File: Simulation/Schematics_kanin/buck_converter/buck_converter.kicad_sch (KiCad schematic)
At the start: 9 parts

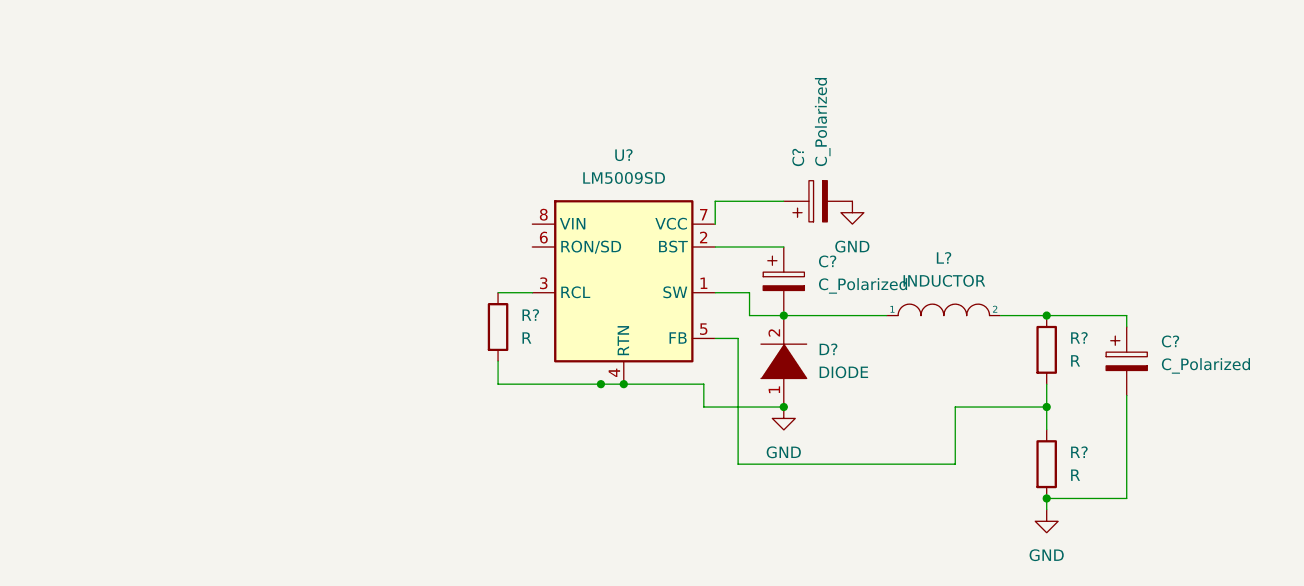
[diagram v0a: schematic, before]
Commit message: Nearly done with 7V MCU ckt, need to size output cap
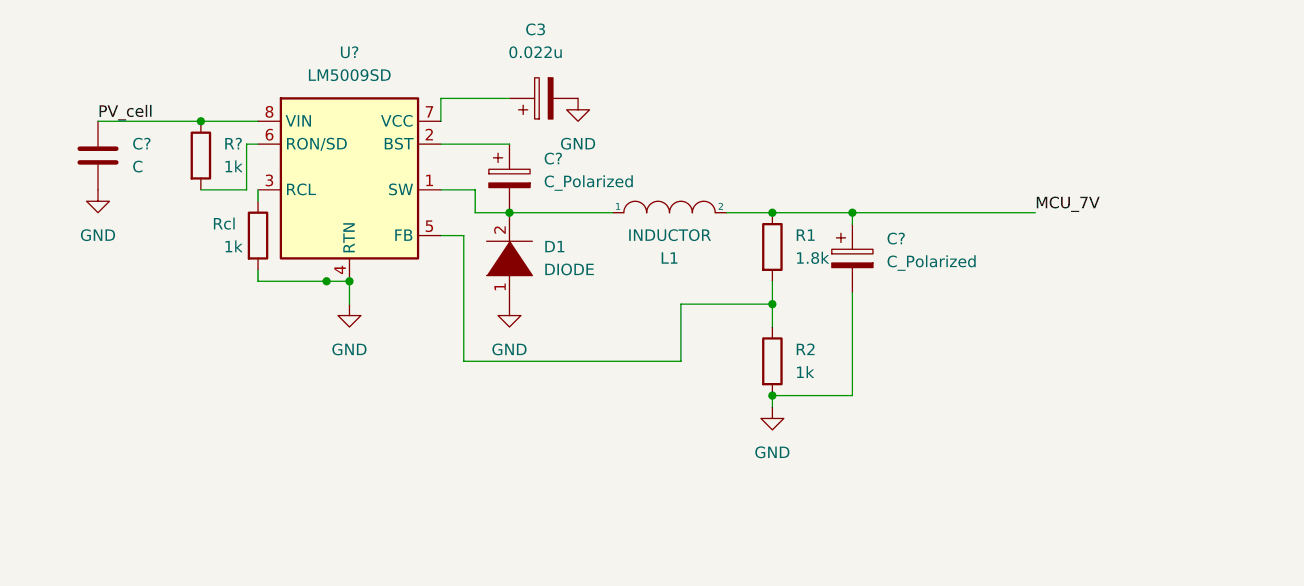
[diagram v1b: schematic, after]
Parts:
- added C?: C, symbol Device:C
- added R?: 1k, symbol Device:R
- C3: renamed from C?; value C_Polarized -> 0.022u
- R1: renamed from R?; value R -> 1.8k
- R2, Rcl: renamed from R?; value R -> 1k
- gave numbers to parts that had none: 2
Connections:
- net GND: now also C?.2
- net at U?.6 (RON/SD): now also R?.2
- net PV_cell: now reaches U?.8 (VIN)
- net PV_cell: now also C?.1, R?.1
- net MCU_7V: now reaches C?.1, L1.2, R1.1
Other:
- moved on the sheet: C3, C?, D1, L1, R1, R2, Rcl, U?

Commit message: Added a few values to schematic
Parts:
- removed C3: 0.022u, symbol Device:C_Polarized
- removed C? (x2): C_Polarized, symbol Device:C_Polarized
- added C2: C, symbol Device:C
- added C3: 0.1u, symbol Device:C
- added C4: 0.022u, symbol Device:C
- C1: renamed from C?; value C -> 0.022u
- gave numbers to parts that had none: 2
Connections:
- net GND: now also C2.2, C3.2
- net MCU_7V: now also C2.1
- net at D1.2 (A), L1.1, U1.1 (SW): now also C4.2
- net at U1.2 (BST): now also C4.1
- net at U1.7 (VCC): now also C3.1
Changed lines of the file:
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@@
     (stroke (width 0) (type default) (color 0 0 0 0))
   )
-  (wire (pts (xy 95.25 128.27) (xy 102.87 128.27))
+  (wire (pts (xy 95.25 128.27) (xy 99.06 128.27))
     (stroke (width 0) (type default) (color 0 0 0 0))
   )
@@
   )
   (wire (pts (xy 102.87 140.97) (xy 114.3 140.97))
+    (stroke (width 0) (type default) (color 0 0 0 0))
+  )
+  (wire (pts (xy 106.68 128.27) (xy 110.49 128.27))
     (stroke (width 0) (type default) (color 0 0 0 0))
   )
@@
   (symbol (lib_id "Regulator_Switching:LM5009SD") (at 85.09 135.89 0) (unit 1)
     (in_bom yes) (on_board yes) (fields_autoplaced)
-    (property "Reference" "U?" (id 0) (at 85.09 123.19 0))
+    (property "Reference" "U1" (id 0) (at 85.09 123.19 0))
     (property "Value" "LM5009SD" (id 1) (at 85.09 125.73 0))
     (property "Footprint" "Package_SON:WSON-8-1EP_4x4mm_P0.8mm_EP2.6x3mm" (id 2) (at 86.36 147.32 0)
@@
   )
   (symbol (lib_id "Device:R") (at 68.58 134.62 0) (unit 1)
-    (in_bom yes) (on_board yes) (fields_autoplaced)
-    (property "Reference" "R?" (id 0) (at 71.12 133.3499 0)
-      (effects (font (size 1.27 1.27)) (justify left))
-    )
-    (property "Value" "1k" (id 1) (at 71.12 135.8899 0)
+    (in_bom yes) (on_board yes)
+    (property "Reference" "Ron" (id 0) (at 63.5 133.3501 0)
+      (effects (font (size 1.27 1.27)) (justify left))
+    )
+    (property "Value" "1k" (id 1) (at 64.77 135.89 0)
       (effects (font (size 1.27 1.27)) (justify left))
     )
@@
     (pin "2")
   )
+  (symbol (lib_id "Device:C") (at 102.87 137.16 0) (unit 1)
+    (in_bom yes) (on_board yes) (fields_autoplaced)
+    (property "Reference" "C4" (id 0) (at 106.68 135.8899 0)
+      (effects (font (size 1.27 1.27)) (justify left))
+    )
+    (property "Value" "0.022u" (id 1) (at 106.68 138.4299 0)
+      (effects (font (size 1.27 1.27)) (justify left))
+    )
+    (property "Footprint" "" (id 2) (at 103.8352 140.97 0)
+      (effects (font (size 1.27 1.27)) hide)
+    )
+    (property "Datasheet" "~" (id 3) (at 102.87 137.16 0)
+      (effects (font (size 1.27 1.27)) hide)
+    )
+    (pin "1")
+    (pin "2")
+  )
   (symbol (lib_id "Device:R") (at 132.08 157.48 0) (unit 1)
     (in_bom yes) (on_board yes) (fields_autoplaced)
@@
     )
     (property "Datasheet" "~" (id 3) (at 132.08 157.48 0)
-      (effects (font (size 1.27 1.27)) hide)
-    )
-    (pin "1")
-    (pin "2")
-  )
-  (symbol (lib_id "Device:C_Polarized") (at 106.68 128.27 90) (unit 1)
-    (in_bom yes) (on_board yes) (fields_autoplaced)
-    (property "Reference" "C3" (id 0) (at 105.791 120.65 90))
-    (property "Value" "0.022u" (id 1) (at 105.791 123.19 90))
-    (property "Footprint" "" (id 2) (at 110.49 127.3048 0)
-      (effects (font (size 1.27 1.27)) hide)
-    )
-    (property "Datasheet" "~" (id 3) (at 106.68 128.27 0)
       (effects (font (size 1.27 1.27)) hide)
     )
@@
   )
   (symbol (lib_id "power:GND") (at 110.49 128.27 0) (unit 1)
-    (in_bom yes) (on_board yes) (fields_autoplaced)
+    (in_bom yes) (on_board yes)
     (property "Reference" "#PWR?" (id 0) (at 110.49 134.62 0)
       (effects (font (size 1.27 1.27)) hide)
     )
-    (property "Value" "GND" (id 1) (at 110.49 133.35 0))
+    (property "Value" "GND" (id 1) (at 114.3 130.81 0))
     (property "Footprint" "" (id 2) (at 110.49 128.27 0)
       (effects (font (size 1.27 1.27)) hide)
@@
     (pin "1")
   )
-  (symbol (lib_id "Device:C_Polarized") (at 140.97 146.05 0) (unit 1)
-    (in_bom yes) (on_board yes) (fields_autoplaced)
-    (property "Reference" "C?" (id 0) (at 144.78 143.8909 0)
-      (effects (font (size 1.27 1.27)) (justify left))
-    )
-    (property "Value" "C_Polarized" (id 1) (at 144.78 146.4309 0)
+  (symbol (lib_id "Device:C") (at 57.15 134.62 0) (unit 1)
+    (in_bom yes) (on_board yes)
+    (property "Reference" "C1" (id 0) (at 52.07 133.35 0)
+      (effects (font (size 1.27 1.27)) (justify left))
+    )
+    (property "Value" "0.022u" (id 1) (at 48.26 135.89 0)
+      (effects (font (size 1.27 1.27)) (justify left))
+    )
+    (property "Footprint" "" (id 2) (at 58.1152 138.43 0)
+      (effects (font (size 1.27 1.27)) hide)
+    )
+    (property "Datasheet" "~" (id 3) (at 57.15 134.62 0)
+      (effects (font (size 1.27 1.27)) hide)
+    )
+    (pin "1")
+    (pin "2")
+  )
+  (symbol (lib_id "Device:R") (at 132.08 144.78 0) (unit 1)
+    (in_bom yes) (on_board yes) (fields_autoplaced)
+    (property "Reference" "R1" (id 0) (at 134.62 143.5099 0)
+      (effects (font (size 1.27 1.27)) (justify left))
+    )
+    (property "Value" "1.8k" (id 1) (at 134.62 146.0499 0)
+      (effects (font (size 1.27 1.27)) (justify left))
+    )
+    (property "Footprint" "" (id 2) (at 130.302 144.78 90)
+      (effects (font (size 1.27 1.27)) hide)
+    )
+    (property "Datasheet" "~" (id 3) (at 132.08 144.78 0)
+      (effects (font (size 1.27 1.27)) hide)
+    )
+    (pin "1")
+    (pin "2")
+  )
+  (symbol (lib_id "Device:C") (at 140.97 146.05 0) (unit 1)
+    (in_bom yes) (on_board yes) (fields_autoplaced)
+    (property "Reference" "C2" (id 0) (at 144.78 144.7799 0)
+      (effects (font (size 1.27 1.27)) (justify left))
+    )
+    (property "Value" "C" (id 1) (at 144.78 147.3199 0)
       (effects (font (size 1.27 1.27)) (justify left))
     )
@@
     )
     (property "Datasheet" "~" (id 3) (at 140.97 146.05 0)
-      (effects (font (size 1.27 1.27)) hide)
-    )
-    (pin "1")
-    (pin "2")
-  )
-  (symbol (lib_id "Device:C") (at 57.15 134.62 0) (unit 1)
-    (in_bom yes) (on_board yes) (fields_autoplaced)
-    (property "Reference" "C?" (id 0) (at 60.96 133.3499 0)
-      (effects (font (size 1.27 1.27)) (justify left))
-    )
-    (property "Value" "C" (id 1) (at 60.96 135.8899 0)
-      (effects (font (size 1.27 1.27)) (justify left))
-    )
-    (property "Footprint" "" (id 2) (at 58.1152 138.43 0)
-      (effects (font (size 1.27 1.27)) hide)
-    )
-    (property "Datasheet" "~" (id 3) (at 57.15 134.62 0)
-      (effects (font (size 1.27 1.27)) hide)
-    )
-    (pin "1")
-    (pin "2")
-  )
-  (symbol (lib_id "Device:C_Polarized") (at 102.87 137.16 0) (unit 1)
-    (in_bom yes) (on_board yes) (fields_autoplaced)
-    (property "Reference" "C?" (id 0) (at 106.68 135.0009 0)
-      (effects (font (size 1.27 1.27)) (justify left))
-    )
-    (property "Value" "C_Polarized" (id 1) (at 106.68 137.5409 0)
-      (effects (font (size 1.27 1.27)) (justify left))
-    )
-    (property "Footprint" "" (id 2) (at 103.8352 140.97 0)
-      (effects (font (size 1.27 1.27)) hide)
-    )
-    (property "Datasheet" "~" (id 3) (at 102.87 137.16 0)
-      (effects (font (size 1.27 1.27)) hide)
-    )
-    (pin "1")
-    (pin "2")
-  )
-  (symbol (lib_id "Device:R") (at 132.08 144.78 0) (unit 1)
-    (in_bom yes) (on_board yes) (fields_autoplaced)
-    (property "Reference" "R1" (id 0) (at 134.62 143.5099 0)
-      (effects (font (size 1.27 1.27)) (justify left))
-    )
-    (property "Value" "1.8k" (id 1) (at 134.62 146.0499 0)
-      (effects (font (size 1.27 1.27)) (justify left))
-    )
-    (property "Footprint" "" (id 2) (at 130.302 144.78 90)
-      (effects (font (size 1.27 1.27)) hide)
-    )
-    (property "Datasheet" "~" (id 3) (at 132.08 144.78 0)
       (effects (font (size 1.27 1.27)) hide)
     )
@@
     (pin "2")
   )
+  (symbol (lib_id "Device:C") (at 102.87 128.27 90) (unit 1)
+    (in_bom yes) (on_board yes)
+    (property "Reference" "C3" (id 0) (at 102.87 121.92 90))
+    (property "Value" "0.1u" (id 1) (at 102.87 124.46 90))
+    (property "Footprint" "" (id 2) (at 106.68 127.3048 0)
+      (effects (font (size 1.27 1.27)) hide)
+    )
+    (property "Datasheet" "~" (id 3) (at 102.87 128.27 0)
+      (effects (font (size 1.27 1.27)) hide)
+    )
+    (pin "1")
+    (pin "2")
+  )
   (symbol (lib_id "power:GND") (at 57.15 138.43 0) (unit 1)
     (in_bom yes) (on_board yes) (fields_autoplaced)
@@
       (reference "#PWR?") (unit 1) (value "GND") (footprint "")
     )
-    (path "/2b553623-782f-4adf-8ef5-39ff5fe8494f"
-      (reference "C3") (unit 1) (value "0.022u") (footprint "")
-    )
-    (path "/a7dbcf5d-7f15-47b8-818f-7472764a1ac7"
-      (reference "C?") (unit 1) (value "C_Polarized") (footprint "")
-    )
     (path "/a9633bd9-0fdb-44ba-9ceb-ffd64f086d8d"
-      (reference "C?") (unit 1) (value "C") (footprint "")
-    )
-    (path "/ad1d94a8-7d85-4004-9ab8-aa55ca511b8a"
-      (reference "C?") (unit 1) (value "C_Polarized") (footprint "")
+      (reference "C1") (unit 1) (value "0.022u") (footprint "")
+    )
+    (path "/b60c5a86-ff42-4e07-986a-6288e10d35ae"
+      (reference "C2") (unit 1) (value "C") (footprint "")
+    )
+    (path "/d1872c09-45dc-4dd4-be97-ec8d2716b39c"
+      (reference "C3") (unit 1) (value "0.1u") (footprint "")
+    )
+    (path "/24b6c681-791b-4ec8-bdac-ba799329088b"
+      (reference "C4") (unit 1) (value "0.022u") (footprint "")
     )
     (path "/c5ad2c2b-7d97-4894-b0f0-e840600224dc"
@@
       (reference "R2") (unit 1) (value "1k") (footprint "")
     )
-    (path "/19dd9902-a96d-455c-9588-4579a9a441e0"
-      (reference "R?") (unit 1) (value "1k") (footprint "")
-    )
     (path "/4895824f-2ab2-4a7c-9d2b-c176b9fab1a0"
       (reference "Rcl") (unit 1) (value "1k") (footprint "")
     )
+    (path "/19dd9902-a96d-455c-9588-4579a9a441e0"
+      (reference "Ron") (unit 1) (value "1k") (footprint "")
+    )
     (path "/0fc5db66-6188-4c1f-bb14-0868bef113eb"
-      (reference "U?") (unit 1) (value "LM5009SD") (footprint "Package_SON:WSON-8-1EP_4x4mm_P0.8mm_EP2.6x3mm")
-    )
-  )
+      (reference "U1") (unit 1) (value "LM5009SD") (footprint "Package_SON:WSON-8-1EP_4x4mm_P0.8mm_EP2.6x3mm")
+    )
+  )

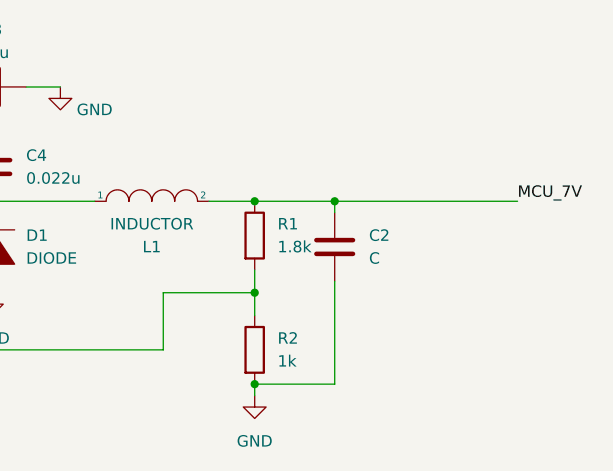
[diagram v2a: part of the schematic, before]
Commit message: Adding new datasheet with LM5009 use cases
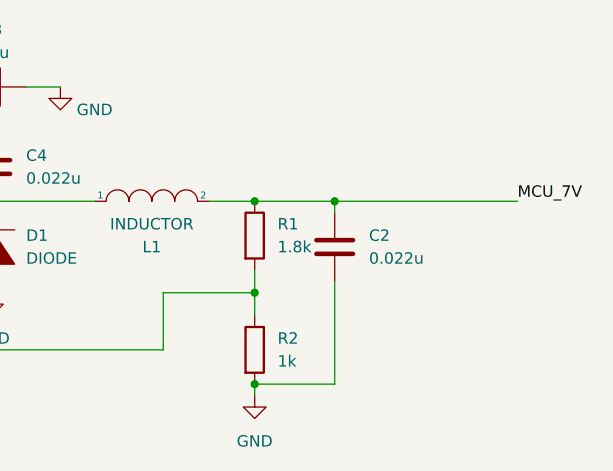
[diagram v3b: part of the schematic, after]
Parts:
- C2: value C -> 0.022u
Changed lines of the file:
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@@
       (effects (font (size 1.27 1.27)) (justify left))
     )
-    (property "Value" "C" (id 1) (at 144.78 147.3199 0)
+    (property "Value" "0.022u" (id 1) (at 144.78 147.3199 0)
       (effects (font (size 1.27 1.27)) (justify left))
     )
@@
     )
     (path "/b60c5a86-ff42-4e07-986a-6288e10d35ae"
-      (reference "C2") (unit 1) (value "C") (footprint "")
+      (reference "C2") (unit 1) (value "0.022u") (footprint "")
     )
     (path "/d1872c09-45dc-4dd4-be97-ec8d2716b39c"

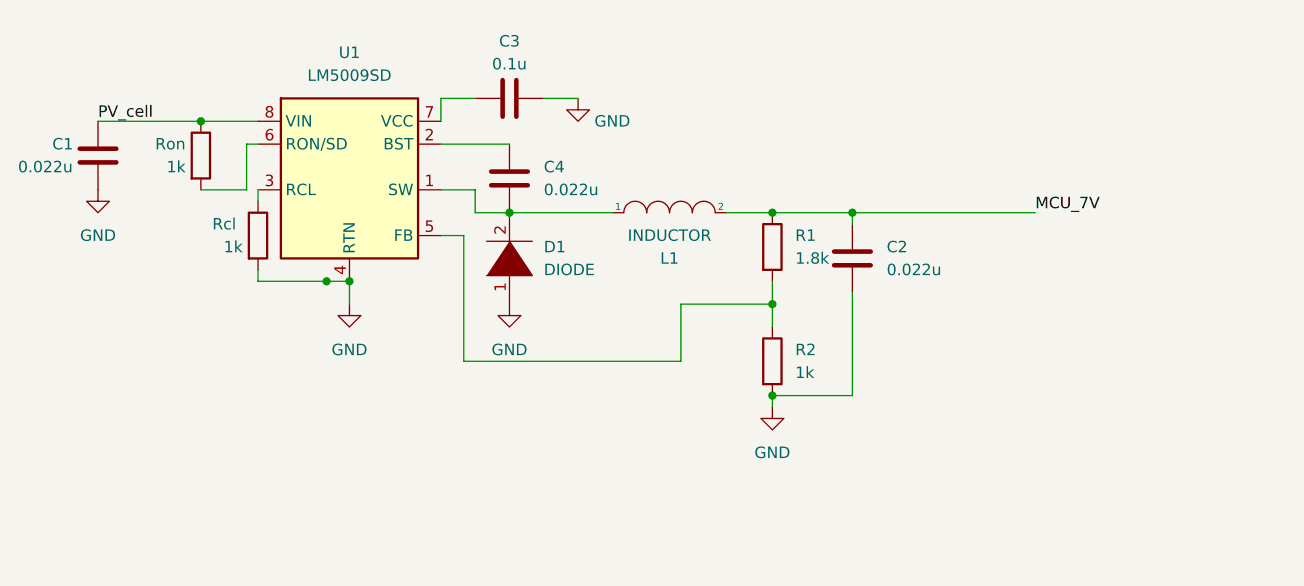
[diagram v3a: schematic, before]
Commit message: Added new design for 7 V output
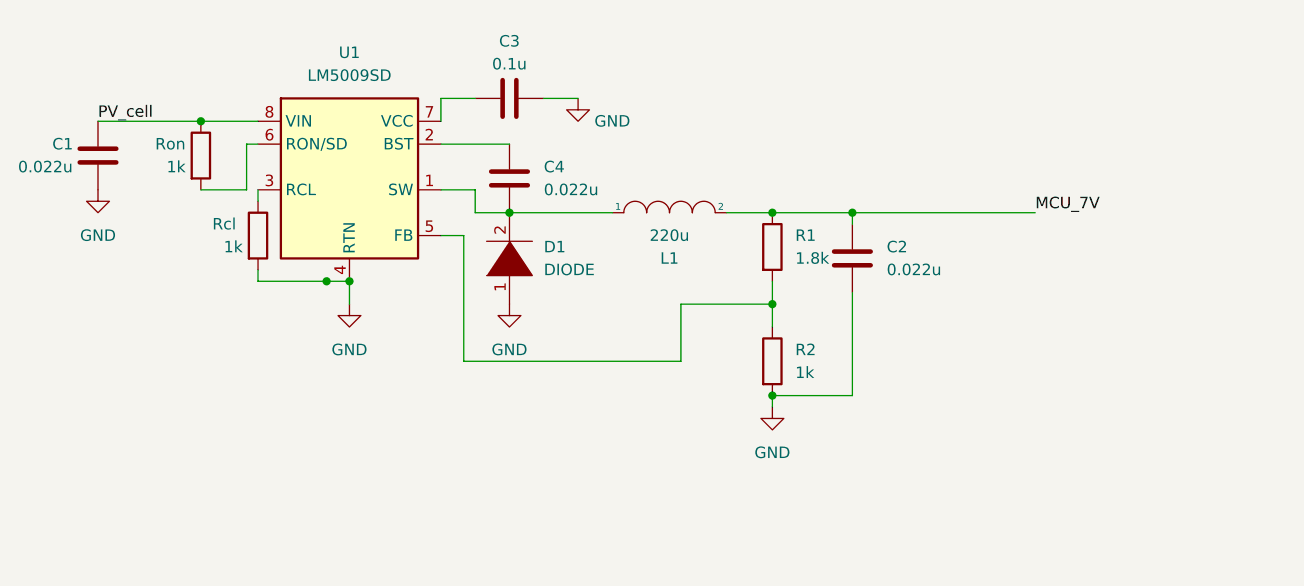
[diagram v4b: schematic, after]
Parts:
- L1: value INDUCTOR -> 220u
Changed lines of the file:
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@@
     (in_bom yes) (on_board yes)
     (property "Reference" "L1" (id 0) (at 120.65 146.05 0))
-    (property "Value" "INDUCTOR" (id 1) (at 120.65 143.51 0))
+    (property "Value" "220u" (id 1) (at 120.65 143.51 0))
     (property "Footprint" "" (id 2) (at 120.65 140.97 0)
       (effects (font (size 1.27 1.27)) hide)
@@
     )
     (path "/767a3c84-8854-4a89-9dfe-d09866d29976"
-      (reference "L1") (unit 1) (value "INDUCTOR") (footprint "")
+      (reference "L1") (unit 1) (value "220u") (footprint "")
     )
     (path "/b32f2e70-da2a-4d9b-ad0c-f3706f6f8f40"
